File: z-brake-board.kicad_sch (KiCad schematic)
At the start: 18 parts, among them J1 to Control Cabinet, J2 to Z Servo, Q2 BTS4142N, U1 LTV-817S, U2 LTV-817S, U3 LTV-817S

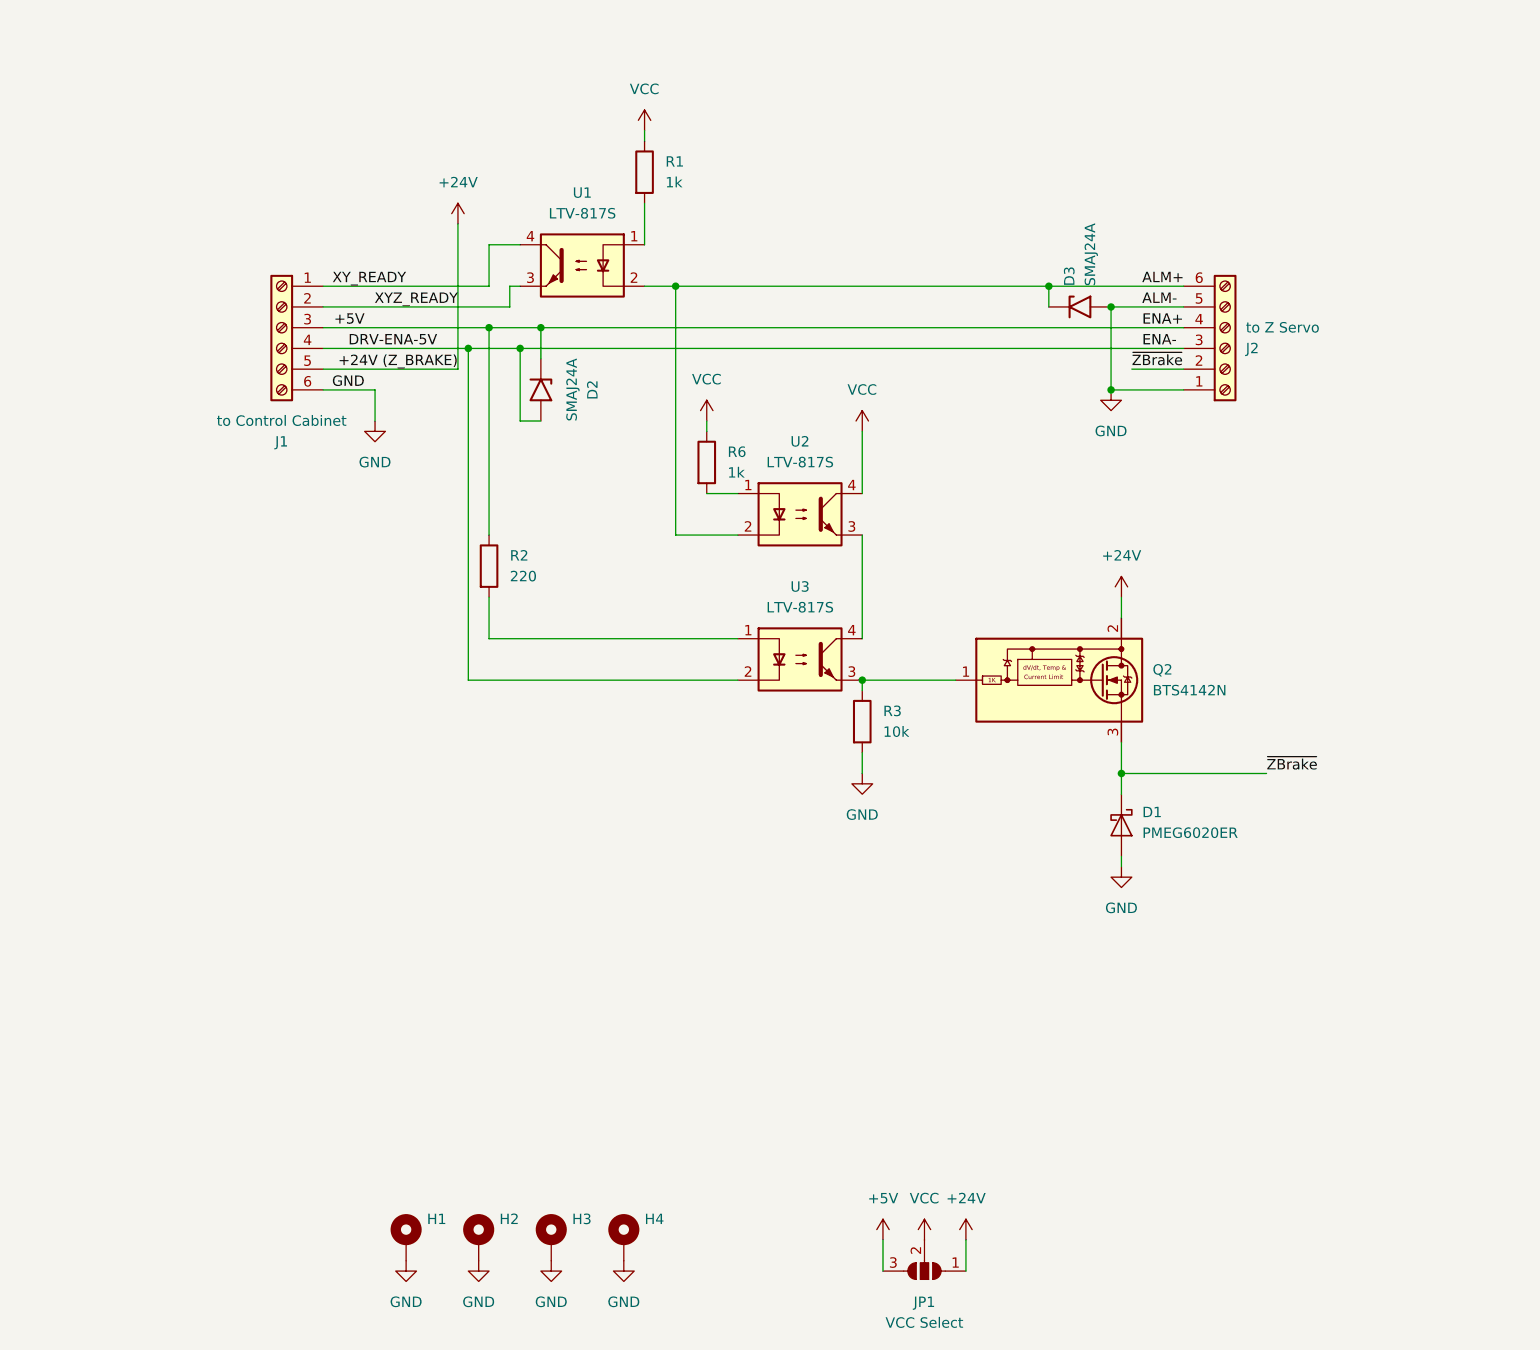
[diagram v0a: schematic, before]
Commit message: Reworked design (less fancy)
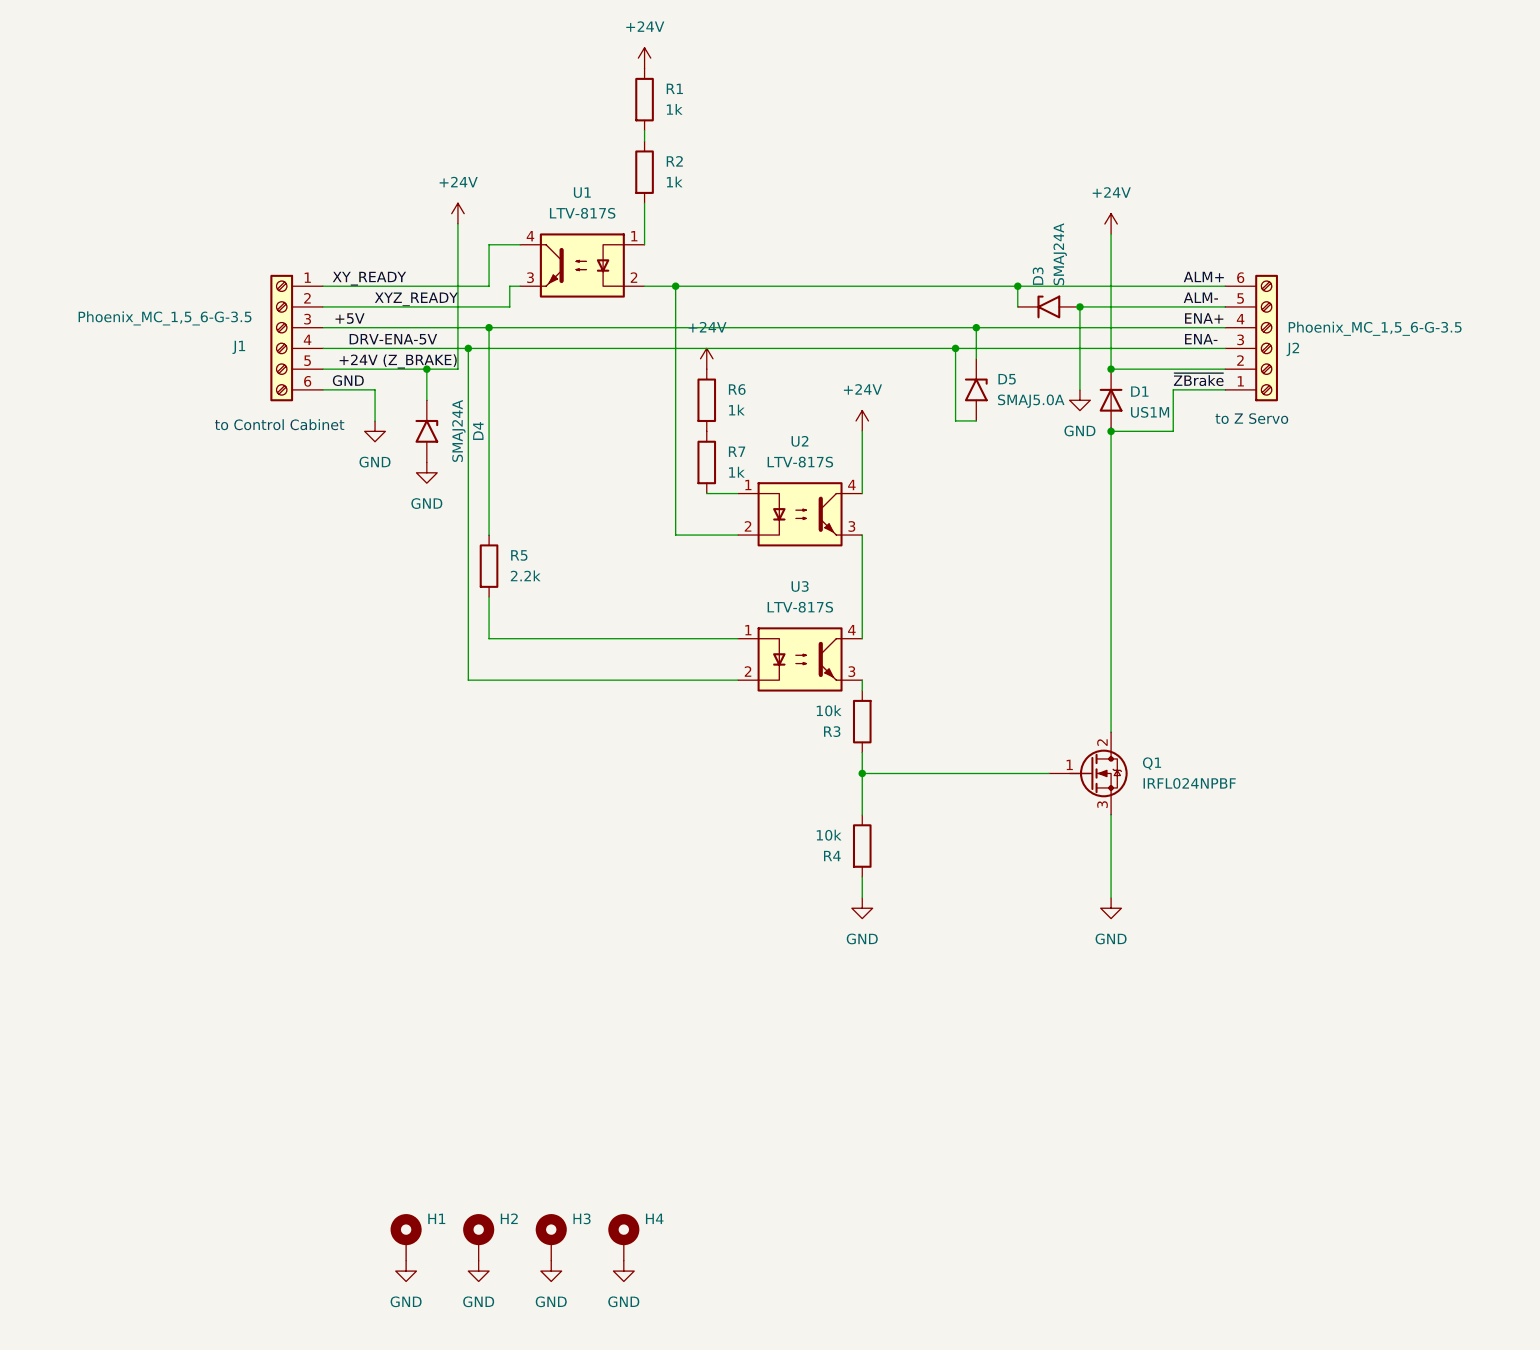
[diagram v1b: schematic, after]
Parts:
- removed D1: PMEG6020ER, Diode_SMD:Nexperia_CFP3_SOD-123W, symbol Diode:PMEG6020ER
- removed D2: SMAJ24A, Diode_SMD:D_SMA, symbol Diode:SMAJ24A
- removed JP1: VCC Select, Jumper:SolderJumper-3_P1.3mm_Open_RoundedPad1.0x1.5mm_NumberLabels, symbol Jumper:SolderJumper_3_Open
- removed Q2: BTS4142N, Package_TO_SOT_SMD:SOT-223, symbol Driver_FET:BTS4140N
- added D1: US1M, Diode_SMD:D_SMA, symbol Diode:US1M
- added D4: SMAJ24A, Diode_SMD:D_SMA, symbol Diode:SMAJ24A
- added D5: SMAJ5.0A, Diode_SMD:D_SMA, symbol Diode:SMAJ5.0A
- added Q1: IRFL024NPBF, Package_TO_SOT_SMD:SOT-223-3_TabPin2, symbol Transistor_FET:BSP129
- added R4: 10k, Resistor_SMD:R_0805_2012Metric_Pad1.20x1.40mm_HandSolder, symbol Device:R
- added R5: 2.2k, Resistor_SMD:R_1206_3216Metric_Pad1.30x1.75mm_HandSolder, symbol Device:R
- added R7: 1k, Resistor_SMD:R_1206_3216Metric_Pad1.30x1.75mm_HandSolder, symbol Device:R
- J1: value to Control Cabinet -> Phoenix_MC_1,5_6-G-3.5
- J2: value to Z Servo -> Phoenix_MC_1,5_6-G-3.5
- R1, R6: footprint Resistor_SMD:R_1210_3225Metric_Pad1.30x2.65mm_HandSolder -> Resistor_SMD:R_1206_3216Metric_Pad1.30x1.75mm_HandSolder
- R2: value 220 -> 1k; footprint Resistor_SMD:R_0805_2012Metric_Pad1.20x1.40mm_HandSolder -> Resistor_SMD:R_1206_3216Metric_Pad1.30x1.75mm_HandSolder
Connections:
- net VCC is gone; now on net +24V: R1.1, R6.1, U2.4
- net +24V: now also J2.2 (Pin_2), D1.1 (K), D4.1 (A1)
- net +5V: now also D5.1 (A1), R5.1; no longer R2.1
- net DRV-ENA-5V: now also D5.2 (A2)
- net GND: now also D4.2 (A2), Q1.3 (S), R4.2; no longer J2.1 (Pin_1), R3.2
- net ~{ZBrake}: now also J2.1 (Pin_1), D1.2 (A), Q1.2 (D); no longer J2.2 (Pin_2)
- net at R2.2: now also U1.1; no longer U3.1
- net at U2.1: now also R7.2; no longer R6.2
- net at R1.2: now also R2.1; no longer U1.1
- net at R3.1: now also Q1.1 (G), R4.1; no longer U3.3
- new net: R5.2, U3.1
- new net: R3.2, U3.3
- new net: R6.2, R7.1
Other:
- note added: "to Control Cabinet"
- note added: "to Z Servo"
- moved on the sheet: D3, J2, R1, R2, R3, R6

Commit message: U2 removed
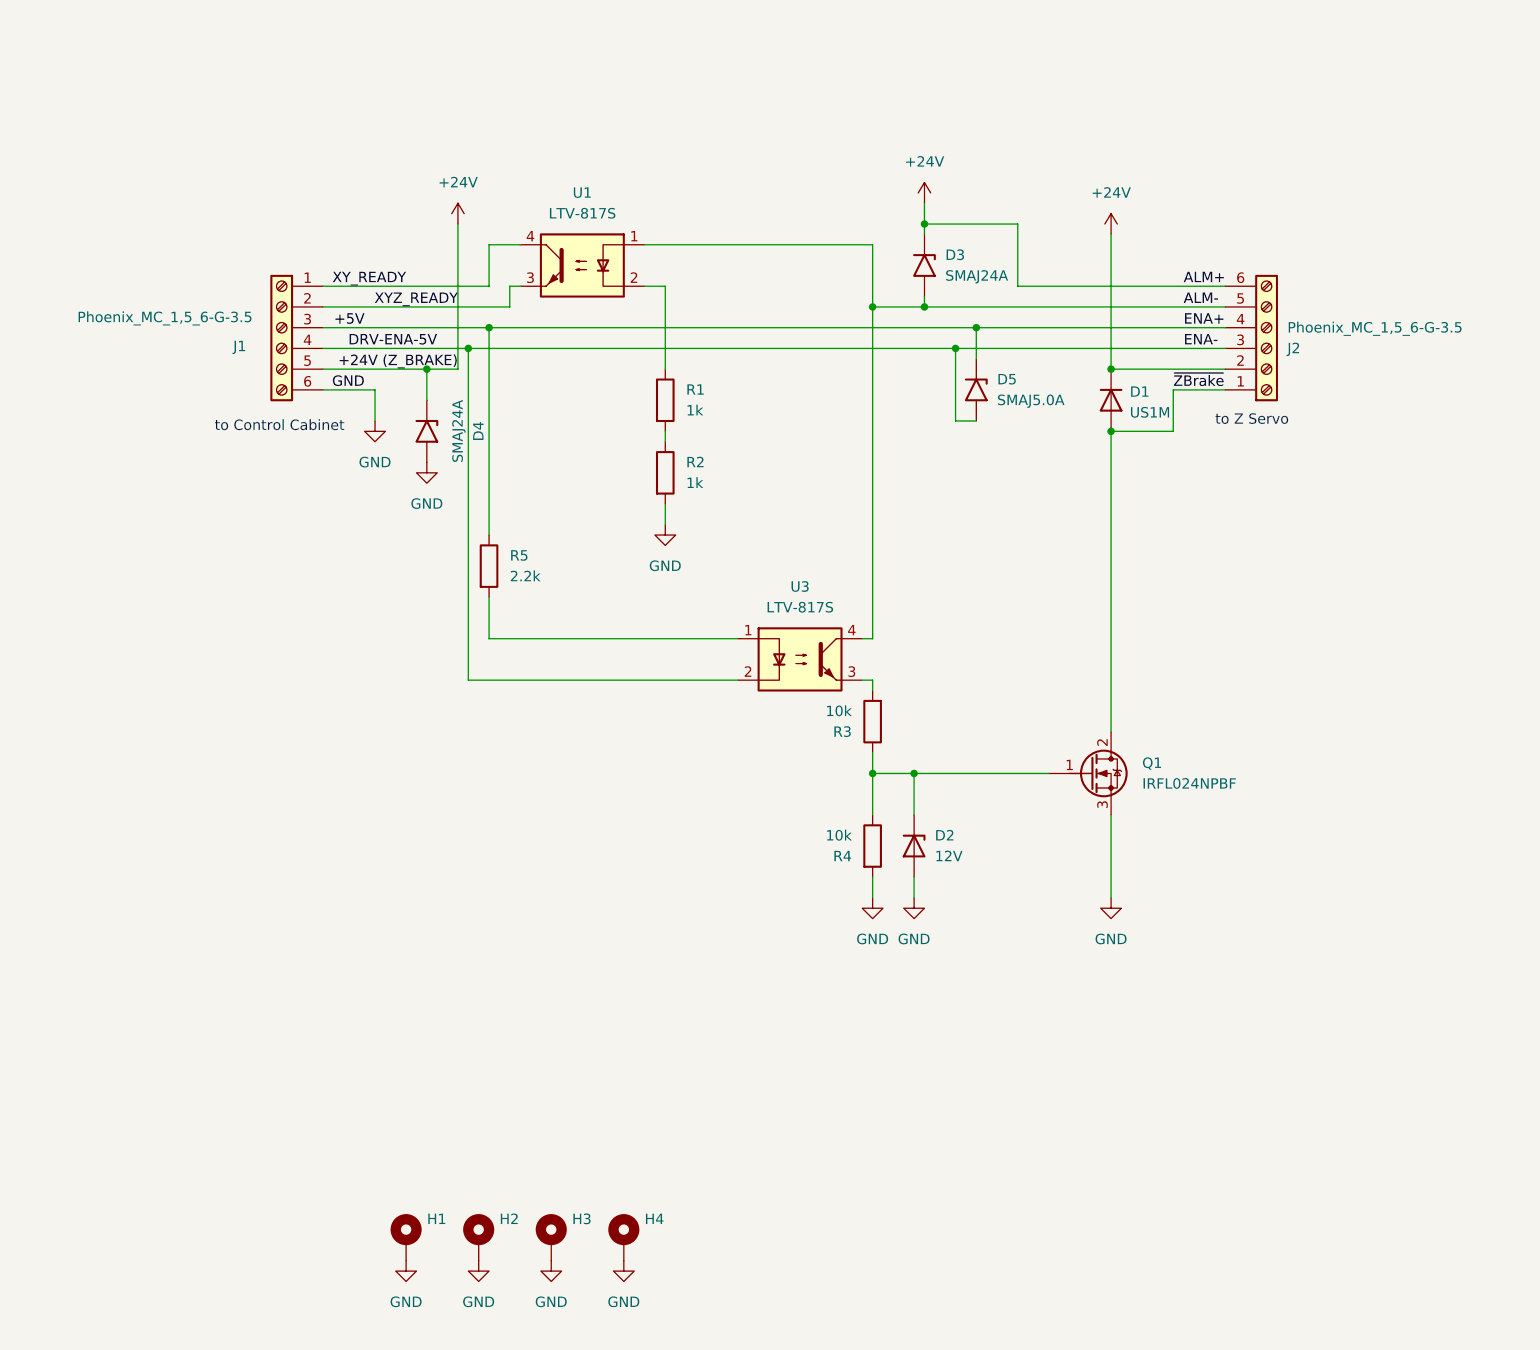
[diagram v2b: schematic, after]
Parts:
- removed R6, R7: 1k, Resistor_SMD:R_1206_3216Metric_Pad1.30x1.75mm_HandSolder, symbol Device:R
- removed U2: LTV-817S, Package_DIP:SMDIP-4_W9.53mm, symbol Isolator:LTV-817S
- added D2: 12V, Diode_SMD:D_SOD-123, symbol Device:D_Zener
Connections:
- net +24V: now also D3.1 (A1), J2.6 (Pin_6); no longer R1.1
- net GND: now also R2.2, D2.2 (A); no longer D3.2 (A2), J2.5 (Pin_5)
- net ALM-: now reaches U1.1
- net ALM-: now also D3.2 (A2), J2.5 (Pin_5), U3.4; no longer R2.2
- net at Q1.1 (G), R3.1, R4.1: now also D2.1 (K)
- removed net ALM+: D3.1 (A1), J2.6 (Pin_6), U1.2
- new net: R1.1, U1.2
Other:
- moved on the sheet: D3, R1, R2, R3, R4

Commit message: Minor cleanups
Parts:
- renumbered U3 to U2
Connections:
- net +24V: no longer J1.2 (Pin_2), U1.3
- new net XYZ_READY: J1.2 (Pin_2), U1.3
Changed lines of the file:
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@@
 	)
 	(label "XYZ_READY"
-		(at 100.33 60.96 180)
+		(at 95.25 60.96 180)
 		(effects
 			(font
@@
 		(dnp no)
 		(fields_autoplaced yes)
-		(property "Reference" "U3"
+		(property "Reference" "U2"
 			(at 142.24 95.25 0)
 			(effects
@@
 			(project "z-brake-board"
 				(path "/e01ab438-817d-4edd-afaa-2c11b95a7855"
-					(reference "U3")
-					(unit 1)
-				)
+					(reference "U2")
+					(unit 1)
+				)
